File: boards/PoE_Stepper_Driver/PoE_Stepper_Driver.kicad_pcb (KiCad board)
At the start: 2 copper layers, 99.1 x 71.1 mm, 133 parts, among them J1 RJ45, J2 Motor, J3 Limits, Q1 NMOS_POE, Q10 NMOS_POE, Q3 NMOS_POE, Q4 NMOS_POE, Q5 NMOS_POE, Q6 NMOS_POE, Q7 NMOS_POE, Q8 NMOS_POE, Q9 NMOS_POE, SW3 SW_Push, U1 LT4321, U14 DP83848C, U15 TMC429-I, U16 TMC2660C-PA, U2 LT4293, U3 STM32F407VETx, U4 NCP1117, U5 E48SC12010, X1 SXO53C, Y1 8MHz

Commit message: done routing phy signals to mcu
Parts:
- removed C10: 0.1uF, Capacitor_SMD:C_0805_2012Metric_Pad1.15x1.40mm_HandSolder
- removed C40: 47uF, Capacitor_THT:CP_Radial_D8.0mm_P3.50mm
- removed C8, C9: 10uF, Capacitor_SMD:CP_Elec_6.3x5.4
- removed D7: Green, LED_SMD:LED_0805_2012Metric_Pad1.15x1.40mm_HandSolder
- removed R39: 470, Resistor_SMD:R_0805_2012Metric_Pad1.15x1.40mm_HandSolder
- removed U4: NCP1117, Package_TO_SOT_SMD:SOT-223-3_TabPin2
- removed U5: E48SC12010, PoE_Stepper_Driver:E48SC12010
- added J4: Programming, Connector_PinHeader_2.54mm:PinHeader_1x04_P2.54mm_Vertical, F.Cu at (61.6, 52.3)
- added J5: 48V In, Connector_PinHeader_2.54mm:PinHeader_1x03_P2.54mm_Vertical, F.Cu at (7.11, 47.2)
- added J6: 12V, 3V3 Out, Connector_PinHeader_2.54mm:PinHeader_1x03_P2.54mm_Vertical, F.Cu at (-19.4, 64.5)
- added J7: PHY Data, Connector_PinHeader_2.54mm:PinHeader_2x04_P2.54mm_Vertical, F.Cu at (96.9, 39.4)
- added J8: SPI Data, Connector_PinHeader_2.54mm:PinHeader_2x05_P2.54mm_Vertical, F.Cu at (117.7, 50.8)
- C14, C17, C18, C2, C23, J2, J3: moved to B.Cu
- moved C17 260.2 mm to (31.1, 69.8), turned to 180 degrees
- moved J2 256.0 mm to (34.4, 75.7), turned to 180 degrees
- moved U16 249.5 mm to (30.9, 62.9), turned to 180 degrees
- moved C18 230.3 mm to (24.0, 70.1), turned to 180 degrees
- moved C23 227.8 mm to (32.8, 56.8)
- moved C21 226.4 mm to (18.4, 65.5), turned to 180 degrees
- moved R28 222.3 mm to (18.7, 55.5)
- moved C22 217.1 mm to (32.1, 103.1)
- moved R27 213.4 mm to (31.4, 50.3)
- moved R26 212.2 mm to (42.2, 56.5)
- moved C15 210.0 mm to (37.2, 53.6)
- moved C16 209.5 mm to (25.5, 53.8)
- moved U15 208.8 mm to (82.8, 71.9), turned to 180 degrees
- moved R29 208.4 mm to (31.4, 53.3)
- moved C20 208.4 mm to (32.2, 107.4)
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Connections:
- D4 pad 1: Net-(D4-Pad1) -> GND
- D5 pad 1: Net-(D4-Pad1) -> GND
- D6 pad 1: Net-(D4-Pad1) -> GND
- U3 pad 1: Net-(U3-Pad1) -> Net-(R1-Pad2)
- U3 pad 2: Net-(U3-Pad2) -> Net-(R2-Pad2)
- U3 pad 3: Net-(U3-Pad3) -> Net-(R38-Pad2)
- U3 pad 59: Net-(R1-Pad2) -> Net-(U3-Pad59)
- U3 pad 60: Net-(R2-Pad2) -> Net-(U3-Pad60)
- U3 pad 61: Net-(R38-Pad2) -> Net-(U3-Pad61)
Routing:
- net TXD1: track 0.00 -> 61.8 mm, vias 0 -> 2
- net TXD0: track 0.00 -> 56.0 mm, vias 0 -> 3
- net TXEN: track 0.00 -> 49.3 mm, vias 0 -> 2
- net RXD0: track 0.00 -> 35.4 mm, vias 0 -> 3
- net MDC: track 0.00 -> 33.6 mm, vias 0 -> 2
- net RXD1: track 0.00 -> 32.2 mm, vias 0 -> 3
- net NRST: track 13.1 -> 42.4 mm, vias 0 -> 2
- net MDIO: track 0.00 -> 28.9 mm, vias 0 -> 3
- net CRS_DV: track 2.89 -> 27.2 mm
- net GND: track 45.3 -> 64.6 mm, vias 18 -> 21
- net PWRGD: track 87.9 -> 71.9 mm
- net +12V: track 11.1 -> 0.00 mm
- net Net-(R1-Pad2): track 0.00 -> 9.61 mm
- net Net-(R2-Pad2): track 0.00 -> 8.59 mm
- net Net-(R38-Pad2): track 0.00 -> 7.14 mm
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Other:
- outline, holes or cut-outs redrawn

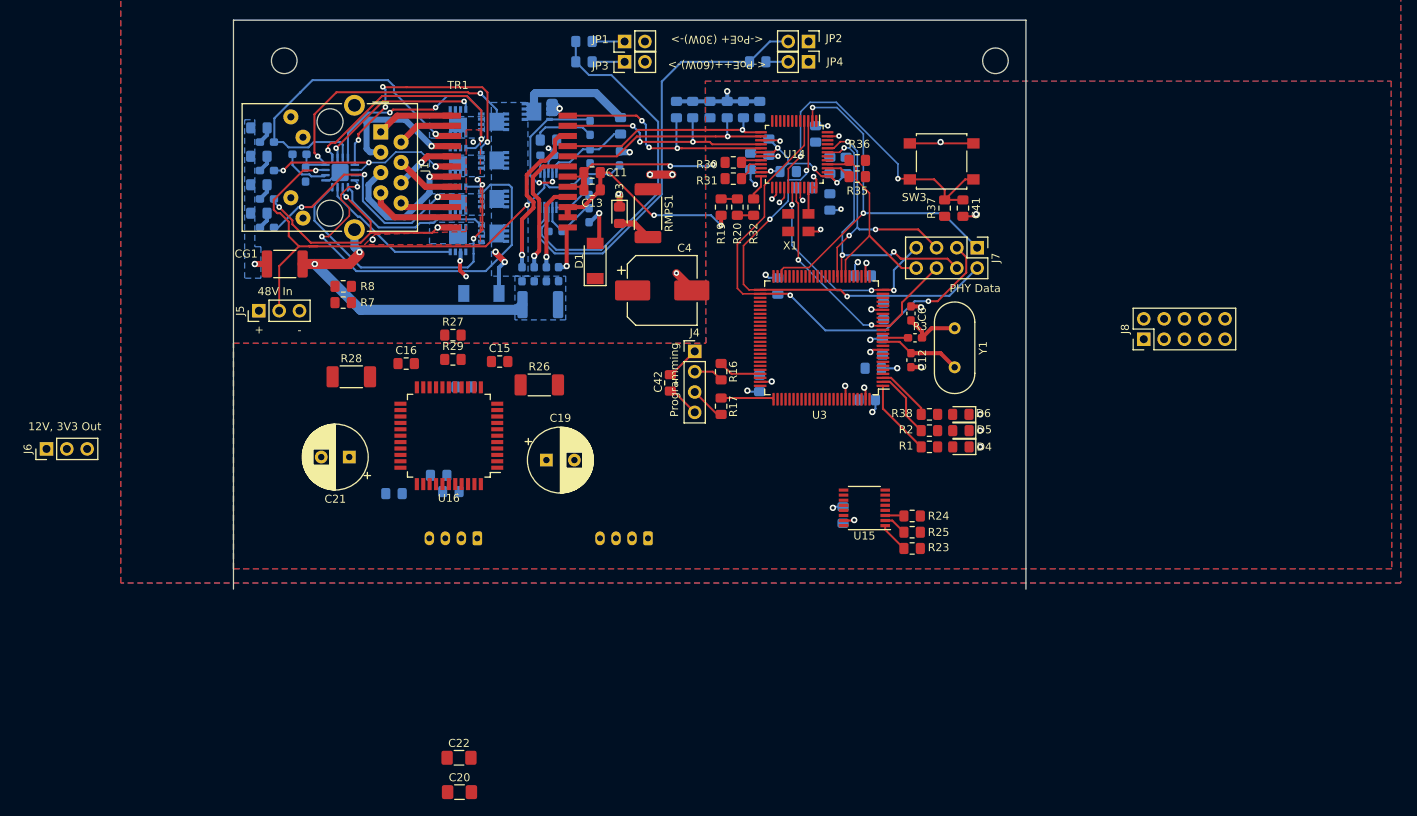
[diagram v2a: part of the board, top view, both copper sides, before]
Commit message: finished 2660 planes
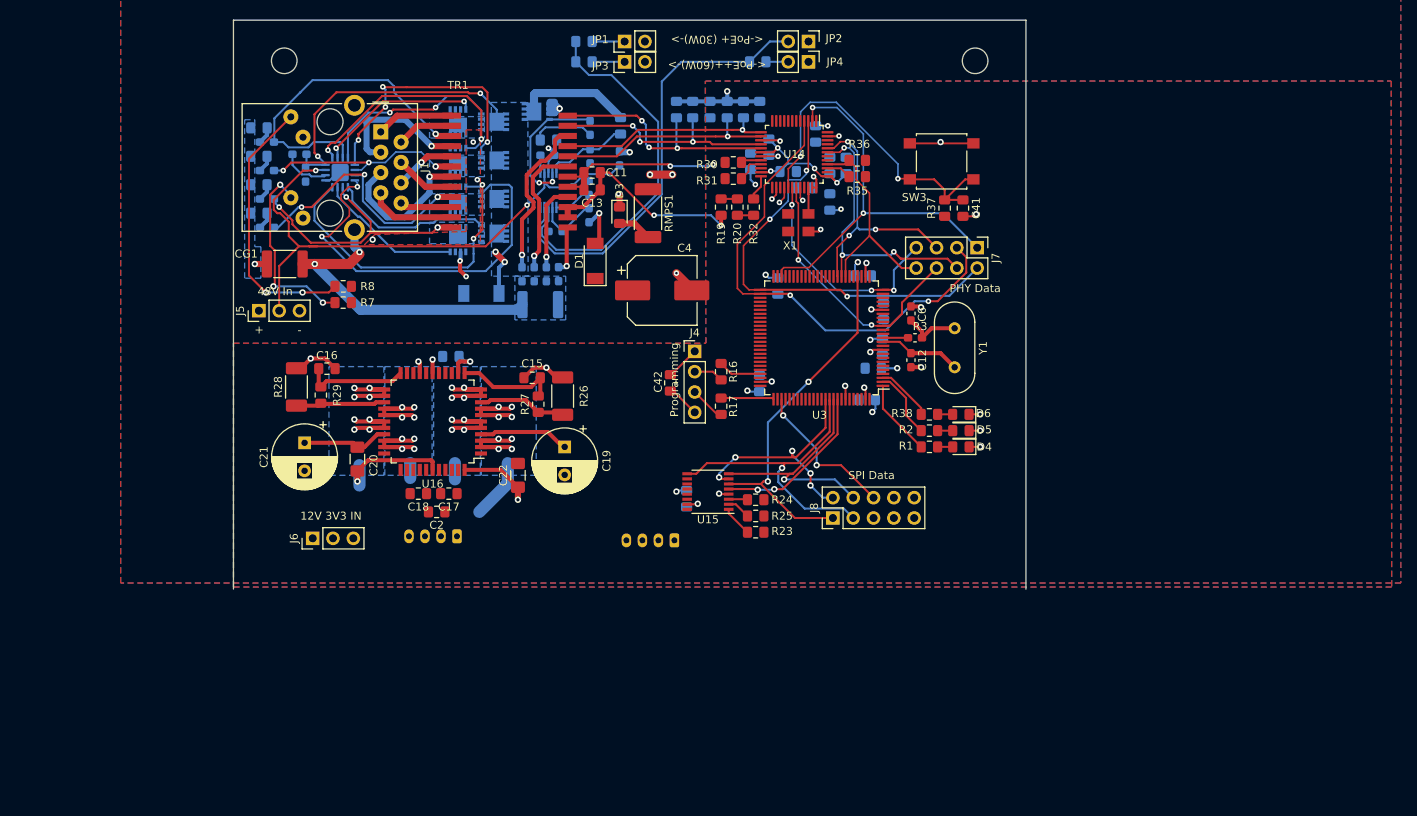
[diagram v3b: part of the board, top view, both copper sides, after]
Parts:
- C17, C18, C2: moved to F.Cu
- J6: value 12V, 3V3 Out -> 12V 3V3 IN
- moved J8 44.8 mm to (78.9, 73.2)
- moved C20 43.5 mm to (19.4, 65.8), turned to 90 degrees
- moved C22 36.1 mm to (39.5, 67.8), turned to 90 degrees
- moved J6 35.1 mm to (13.8, 75.7)
- moved U15 19.7 mm to (63.2, 69.8)
- moved C14 19.7 mm to (60.6, 70.7)
- moved R25 19.7 mm to (69.2, 72.9)
- moved R23 19.7 mm to (69.2, 74.9)
- moved R24 19.7 mm to (69.2, 70.9)
- moved R29 17.1 mm to (14.9, 57.8), turned to 90 degrees
- moved R27 13.7 mm to (42.0, 58.9), turned to 90 degrees
- moved C16 9.93 mm to (15.6, 54.5)
- moved R28 6.97 mm to (11.8, 56.8), turned to 90 degrees
- moved C21 5.86 mm to (12.8, 63.8), turned to 270 degrees
- moved C2 4.58 mm to (29.3, 72.4)
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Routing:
- net SPI1_CS: track 0.00 -> 46.1 mm, vias 0 -> 2
- net GND: track 64.6 -> 109.0 mm, vias 21 -> 28
- net SPI1_MISO: track 0.00 -> 38.0 mm, vias 0 -> 1
- net Net-(J2-Pad1): track 0.00 -> 34.5 mm, vias 0 -> 8
- net Net-(J1-Pad9): track 0.00 -> 33.9 mm, vias 0 -> 2
- net SPI1_SCK: track 0.00 -> 30.6 mm, vias 0 -> 5
- net SPI1_MOSI: track 0.00 -> 30.4 mm, vias 0 -> 1
- net Net-(J2-Pad2): track 0.00 -> 28.4 mm, vias 0 -> 8
- net Net-(J2-Pad3): track 0.00 -> 28.2 mm, vias 0 -> 8
- net Net-(J2-Pad4): track 0.00 -> 24.5 mm, vias 0 -> 8
- net Net-(J1-Pad11): track 0.00 -> 24.3 mm, vias 0 -> 3
- net +12V: track 0.00 -> 22.2 mm
- net CLK_429: track 0.00 -> 20.9 mm, vias 0 -> 2
- net SPI2_SCK: track 0.00 -> 18.9 mm, vias 0 -> 2
- net Net-(C16-Pad1): track 0.00 -> 13.1 mm
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- added copper zone on B.Cu, net Net-(J2-Pad1)
- added copper zone on B.Cu, net Net-(J2-Pad2)
- added copper zone on B.Cu, net Net-(J2-Pad3)
- added copper zone on B.Cu, net Net-(J2-Pad4)

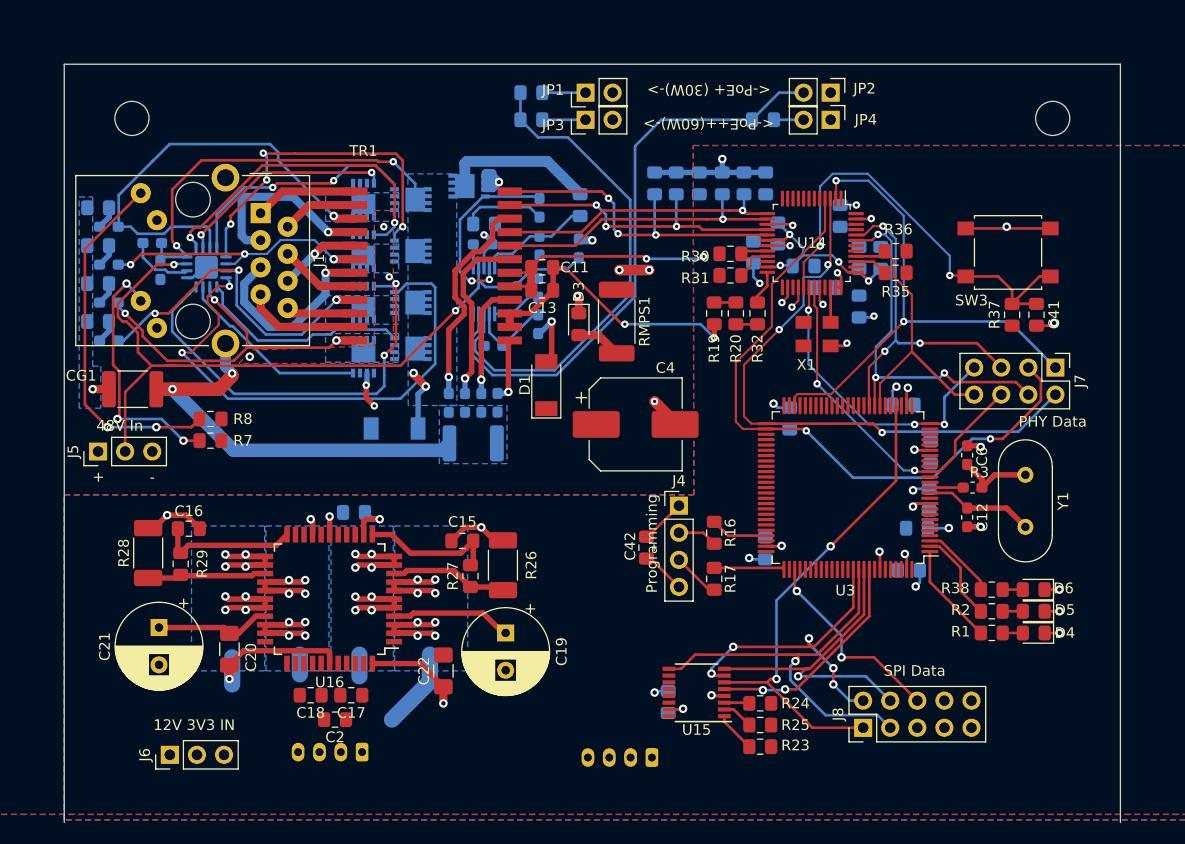
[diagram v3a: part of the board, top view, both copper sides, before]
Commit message: finished spi routing
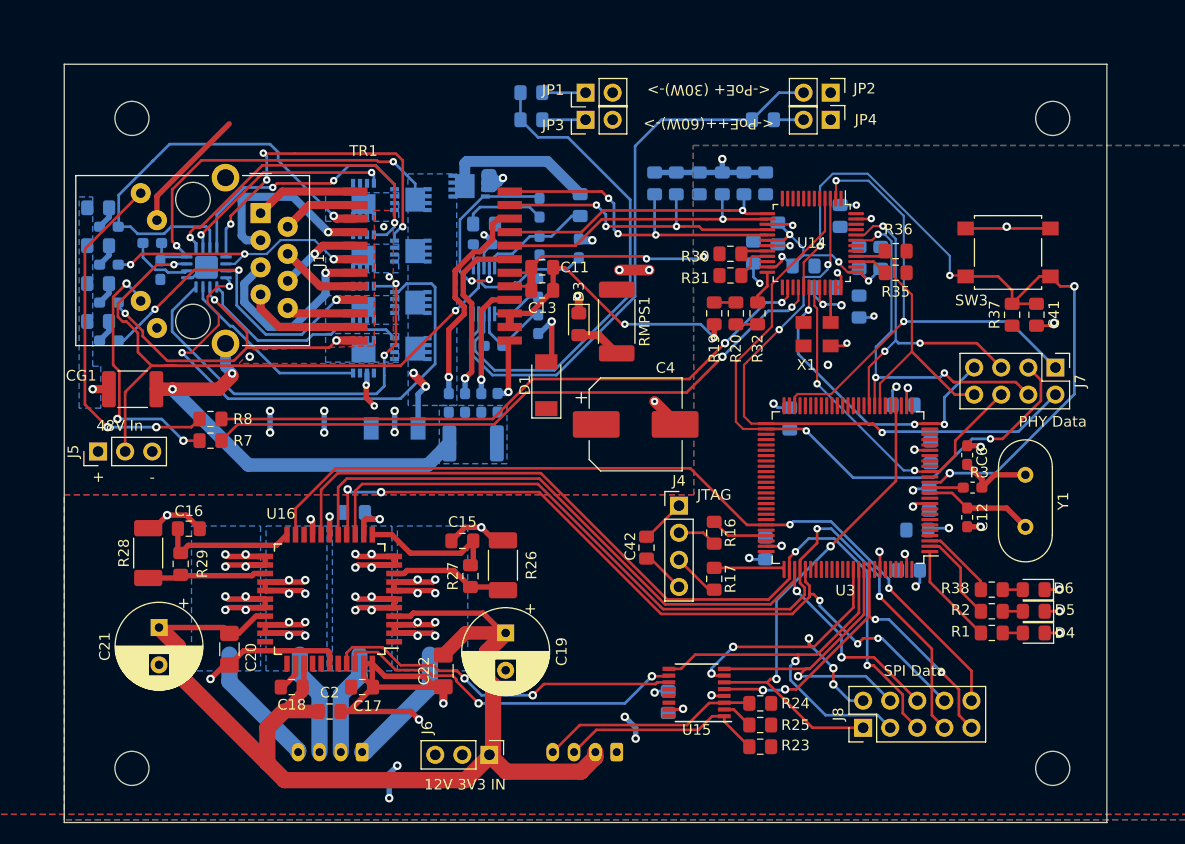
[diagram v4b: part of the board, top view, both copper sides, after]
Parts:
- added REF**: MountingHole_3.2mm_M3, MountingHole:MountingHole_3.2mm_M3, F.Cu at (10.3, 77.0)
- added REF**: MountingHole_3.2mm_M3, MountingHole:MountingHole_3.2mm_M3, F.Cu at (96.6, 77.0)
- J4: value Programming -> JTAG
- moved J6 30.0 mm to (43.8, 75.7), turned to 270 degrees
- moved J3 3.34 mm to (55.8, 75.4)
- moved C18 1.93 mm to (25.3, 69.3)
- moved C17 1.27 mm to (31.9, 69.3), turned to 0 degrees
- moved C2 0.92 mm to (28.8, 71.6)
- moved C39 0.17 mm to (83.9, 54.6)
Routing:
- net +12V: track 22.2 -> 107.4 mm
- net SPI2_MISO: track 0.00 -> 83.4 mm, vias 0 -> 2
- net SPI2_CS: track 0.00 -> 82.7 mm, vias 0 -> 2
- net CLK_2660: track 0.00 -> 78.8 mm, vias 0 -> 2
- net SPI2_MOSI: track 0.00 -> 73.4 mm, vias 0 -> 5
- net /Ethernet/LED_LINK: track 2.11 -> 60.8 mm, vias 1 -> 2
- net /Ethernet/LED_ACT: track 1.65 -> 58.7 mm, vias 1 -> 2
- net SPI2_SCK: track 18.9 -> 73.3 mm
- net /Motor_Control/DIR: track 0.00 -> 34.0 mm, vias 0 -> 2
- net /Motor_Control/STEP: track 0.00 -> 33.6 mm, vias 0 -> 2
- net NRST: track 42.4 -> 72.2 mm, vias 2 -> 4
- net GND: track 109.0 -> 131.4 mm, vias 28 -> 29
- net +3V3: track 57.7 -> 79.1 mm, vias 14 -> 20
- net Net-(J3-Pad4): track 2.37 -> 20.4 mm
- net Net-(J3-Pad3): track 3.83 -> 19.3 mm
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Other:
- board size 99.1 x 71.1 mm -> 97.8 x 71.1 mm

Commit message: finished 1st draft of pcb
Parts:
- moved C33 0.36 mm to (78.7, 33.9)
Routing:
- net +3V3: track 79.1 -> 158.9 mm, vias 20 -> 25
- net VOUT-: track 13.3 -> 31.6 mm, vias 9 -> 13
- net TXD0: track 56.0 -> 68.4 mm, vias 3 -> 5
- net VOUT+: track 17.0 -> 22.8 mm, vias 9 -> 13
- net NRST: track 72.2 -> 69.4 mm
- net GND: track 131.4 -> 133.2 mm, vias 29 -> 31
- net /Ethernet/POE_CT12: track 41.5 -> 43.1 mm
- net Net-(C26-Pad1): track 21.6 -> 23.1 mm
- net CRS_DV: track 27.2 -> 27.8 mm

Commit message: added silkscreen info
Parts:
- removed the REF** at (10.3, 77.0)
- removed the REF** at (96.6, 77.0)
- added R40: 10k, Resistor_SMD:R_0805_2012Metric_Pad1.15x1.40mm_HandSolder, B.Cu at (174.4, 109.1)
- added REF**: MountingHole_3.2mm_M3, MountingHole:MountingHole_3.2mm_M3, F.Cu at (100.1, 123.8)
- added REF**: MountingHole_3.2mm_M3, MountingHole:MountingHole_3.2mm_M3, F.Cu at (186.4, 123.8)
- added TP1: BOOT0, TestPoint:TestPoint_Pad_1.0x1.0mm, B.Cu at (174.8, 111.4)
- C42: moved to B.Cu
- J4: value JTAG -> Programming
- J6: value 12V 3V3 IN -> 12V, 3V3 Out
- moved C26 101.3 mm to (163.1, 76.7)
- moved C31 101.3 mm to (166.5, 72.0)
- moved C38 101.3 mm to (173.0, 105.2)
- moved CG2 101.3 mm to (132.1, 93.3)
- moved J6 101.3 mm to (133.6, 122.6)
- moved JP1 101.3 mm to (142.6, 60.5)
- moved JP3 101.3 mm to (142.6, 63.0)
- moved Q1 101.3 mm to (131.7, 69.2)
- moved Q10 101.3 mm to (121.8, 85.2)
- moved Q4 101.3 mm to (121.8, 80.1)
- moved Q6 101.3 mm to (121.8, 75.3)
- moved Q8 101.3 mm to (121.8, 70.5)
- moved R10 101.3 mm to (134.0, 84.2)
- moved R33 101.3 mm to (149.1, 69.0)
- moved R6 101.3 mm to (159.3, 63.0)
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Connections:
- U3 pad 94: GND -> Net-(R40-Pad1)
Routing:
- net Net-(R40-Pad1): track 0.00 -> 11.7 mm, vias 0 -> 2
- net GND: track 133.2 -> 127.3 mm, vias 31 -> 30

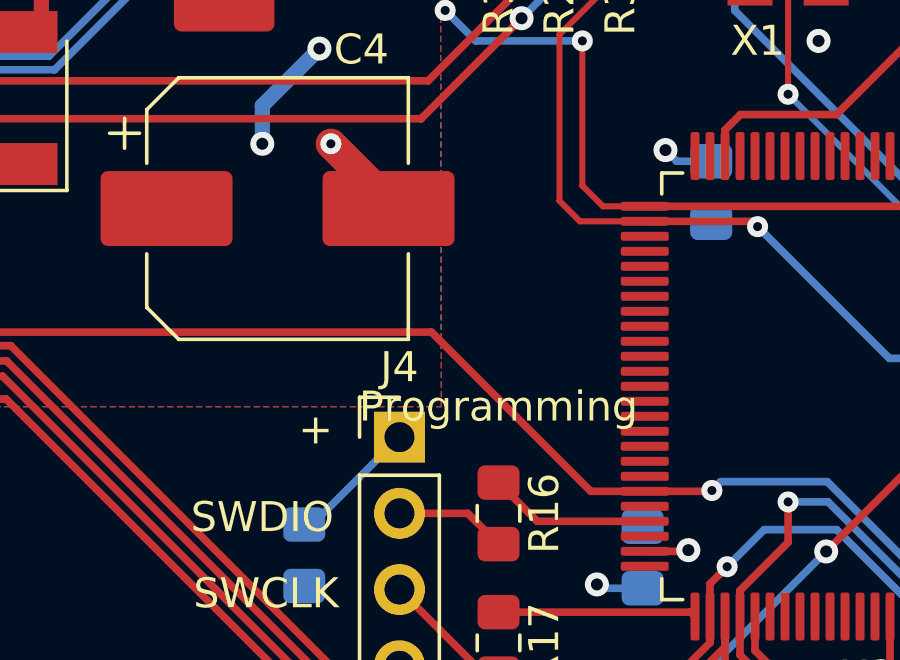
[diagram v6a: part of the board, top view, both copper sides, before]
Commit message: added UART
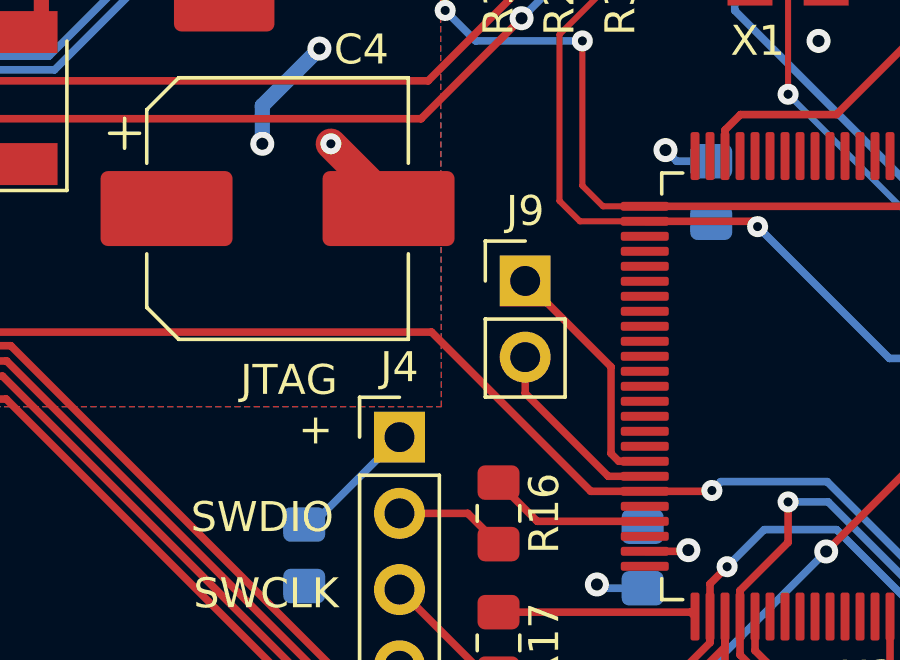
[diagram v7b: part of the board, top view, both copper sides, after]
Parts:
- added J9: UART, Connector_PinHeader_2.54mm:PinHeader_1x02_P2.54mm_Vertical, F.Cu at (155.6, 94.0)
- J4: value Programming -> JTAG
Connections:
- U3 pad 68: Net-(U3-Pad68) -> /UART_TX
- U3 pad 69: Net-(U3-Pad69) -> /UART_RX
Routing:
- net /UART_TX: track 0.00 -> 8.17 mm
- net /UART_RX: track 0.00 -> 6.34 mm
